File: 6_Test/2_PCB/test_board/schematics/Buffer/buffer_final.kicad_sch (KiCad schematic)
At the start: 24 parts, among them J11 Buffer_PWR_Jumper, U7 SN74ALVCH162827DLR

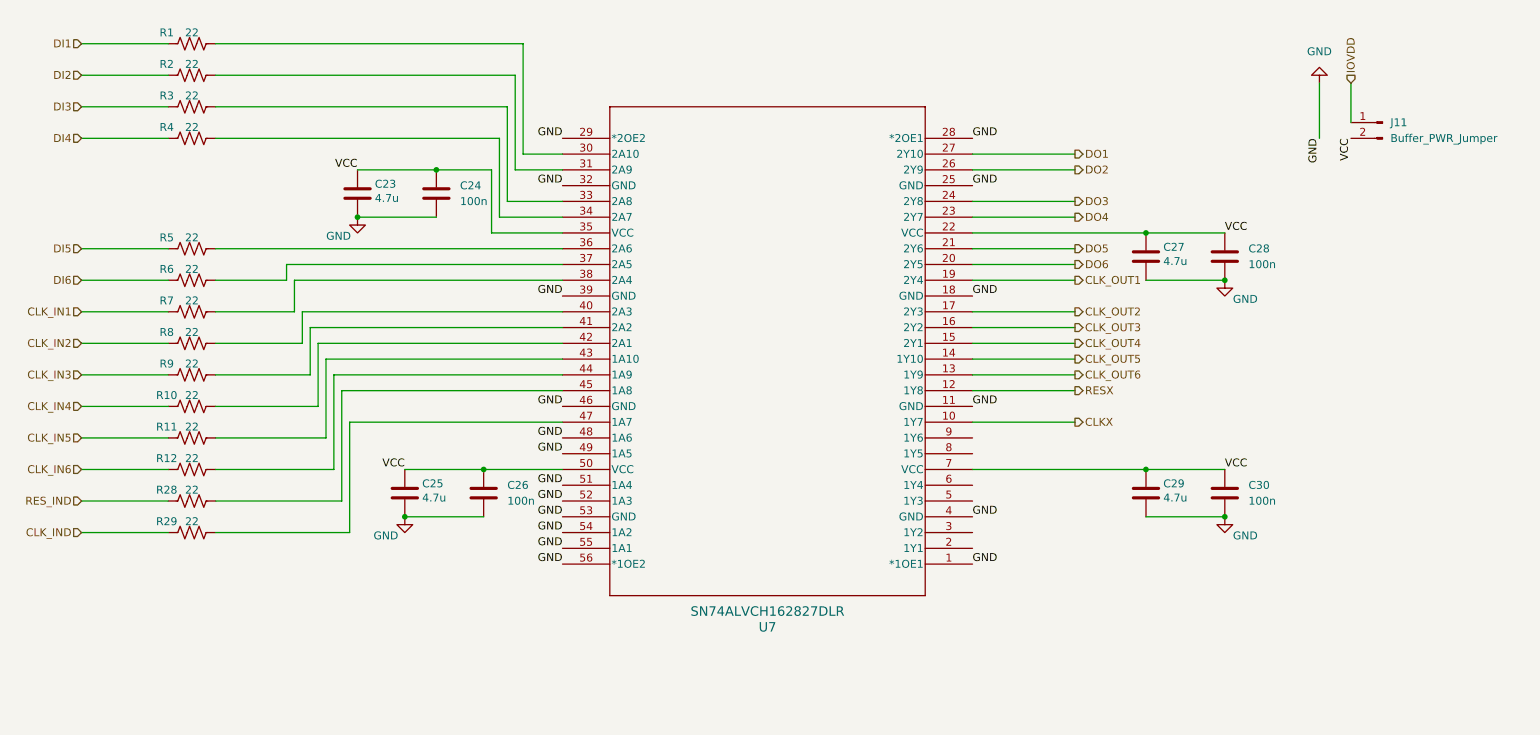
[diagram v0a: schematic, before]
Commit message: Edit Layout 1_27
Rearranged the components in the layout and added majority of traces and ground layer. AVSS connections still need to be connected along with IOVDD
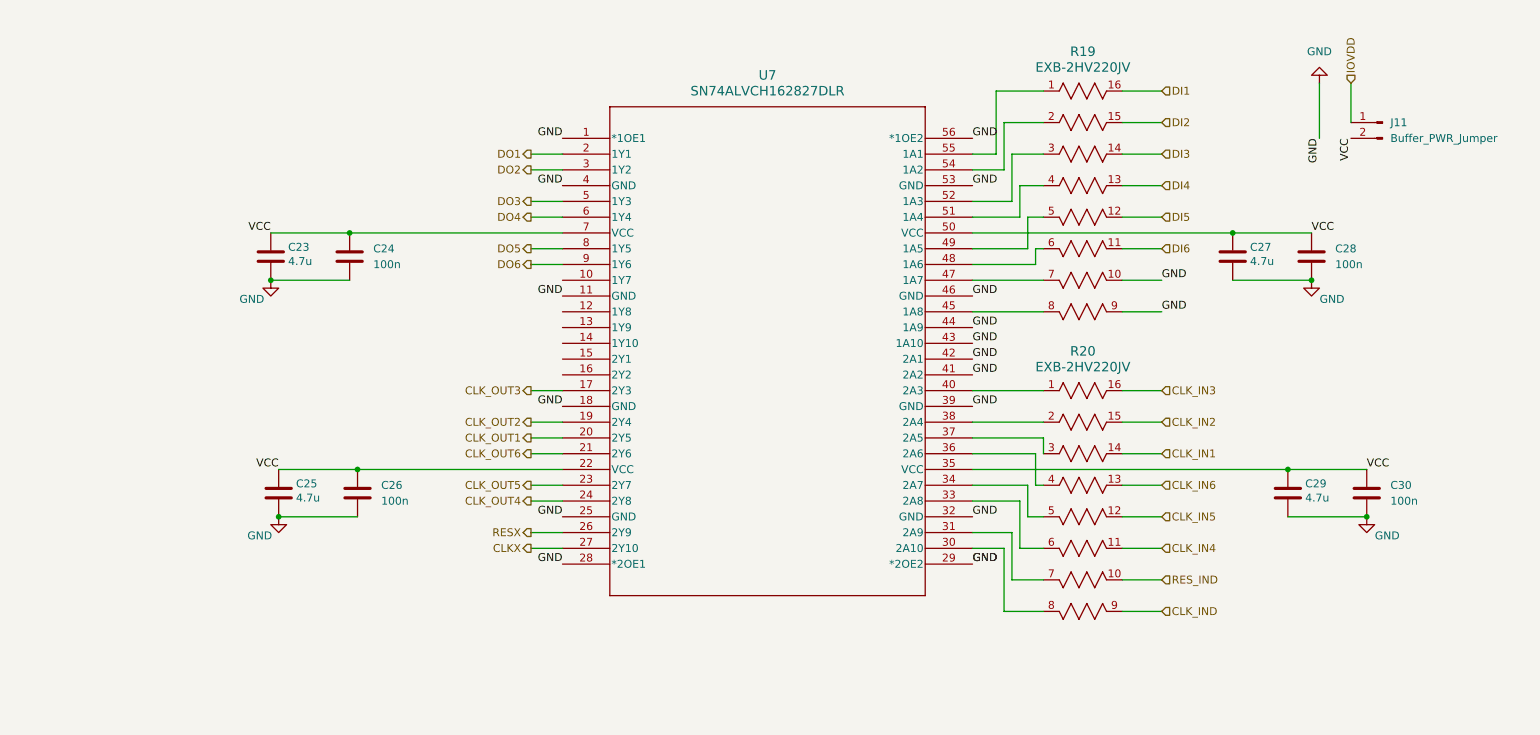
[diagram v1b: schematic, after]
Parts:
- removed R1, R10, R11, R12, R2, R28, R29, R3, R4, R5, R6, R7, R8, R9: 22, Resistor_SMD:R_0402_1005Metric, symbol Device:R_US
- added R19, R20: EXB-2HV220JV, 22res_arrayFootprints:RES_EXB2HV, symbol 22res_array:EXB-2HV220JV
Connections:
- net CLKX: now also U7.27 (2Y10); no longer U7.10 (1Y7)
- net CLK_IN1: now also R20.14
- net CLK_IN2: now also R20.15
- net CLK_IN3: now also R20.16
- net CLK_IN4: now also R20.11
- net CLK_IN5: now also R20.12
- net CLK_IN6: now also R20.13
- net CLK_IND: now also R20.9
- net CLK_OUT1: now also U7.20 (2Y5); no longer U7.19 (2Y4)
- net CLK_OUT2: now also U7.19 (2Y4); no longer U7.17 (2Y3)
- net CLK_OUT3: now also U7.17 (2Y3); no longer U7.16 (2Y2)
- net CLK_OUT4: now also U7.24 (2Y8); no longer U7.15 (2Y1)
- net CLK_OUT5: now also U7.23 (2Y7); no longer U7.14 (1Y10)
- net CLK_OUT6: now also U7.21 (2Y6); no longer U7.13 (1Y9)
- net DI1: now also R19.16
- net DI2: now also R19.15
- net DI3: now also R19.14
- net DI4: now also R19.13
- net DI5: now also R19.12
- net DI6: now also R19.11
- net DO1: now also U7.2 (1Y1); no longer U7.27 (2Y10)
- net DO2: now also U7.3 (1Y2); no longer U7.26 (2Y9)
- net DO3: now also U7.5 (1Y3); no longer U7.24 (2Y8)
- net DO4: now also U7.6 (1Y4); no longer U7.23 (2Y7)
- net DO5: now also U7.8 (1Y5); no longer U7.21 (2Y6)
- net DO6: now also U7.9 (1Y6); no longer U7.20 (2Y5)
- net GND: now also U7.41 (2A2), U7.42 (2A1), U7.43 (1A10), U7.44 (1A9), R19.10, R19.9; no longer U7.48 (1A6), U7.49 (1A5), U7.51 (1A4), U7.52 (1A3), U7.54 (1A2), U7.55 (1A1)
- net RESX: now also U7.26 (2Y9); no longer U7.12 (1Y8)
- net RES_IND: now also R20.10
- net at U7.31 (2A9): now also R20.7
- net at U7.30 (2A10): now also R20.8
- net at U7.33 (2A8): now also R20.6
- net at U7.34 (2A7): now also R20.5
- net at U7.36 (2A6): now also R20.4
- net at U7.37 (2A5): now also R20.3
- net at U7.38 (2A4): now also R20.2
- net at U7.40 (2A3): now also R20.1
- net at U7.45 (1A8): now also R19.8
- net at U7.47 (1A7): now also R19.7
- new net: R19.6, U7.48 (1A6)
- new net: R19.5, U7.49 (1A5)
- new net: R19.4, U7.51 (1A4)
- new net: R19.3, U7.52 (1A3)
- new net: R19.2, U7.54 (1A2)
- new net: R19.1, U7.55 (1A1)
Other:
- moved on the sheet: C23, C24, C25, C26, C27, C28, C29, C30, U7

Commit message: Finished board layout
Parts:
- removed C27, C29: 4.7u, Capacitor_SMD:C_0603_1608Metric, symbol Device:C
- removed C28, C30: 100n, Capacitor_SMD:C_0402_1005Metric, symbol Device:C
- removed U7: SN74ALVCH162827DLR, 74ALVCHFootprints:DL56, symbol 74ALVCH:SN74ALVCH162827DLR
- added R21, R22: EXB-2HV220JV, 22res_arrayFootprints:RES_EXB2HV, symbol 22res_array:EXB-2HV220JV
- added U7: SN74LVC245APWR, SN74LVC245APWRFootprints:PW20, symbol SN74LVC245APWR:SN74LVC245APWR
- added U8: SN74LVC245APWR, PW20, symbol SN74LVC245APWR:SN74LVC245APWR
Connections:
- net CLKX: now also R20.8
- net CLK_IN1: now also R22.14; no longer R20.14
- net CLK_IN2: now also R22.15; no longer R20.15
- net CLK_IN3: now also R22.16; no longer R20.16
- net CLK_IN4: now also R22.11; no longer R20.11
- net CLK_IN5: now also R22.12; no longer R20.12
- net CLK_IN6: now also R22.13; no longer R20.13
- net CLK_IND: now also R22.9; no longer R20.9
- net CLK_OUT1: now also R20.3
- net CLK_OUT2: now also R20.2
- net CLK_OUT3: now also R20.1
- net CLK_OUT4: now also R20.6
- net CLK_OUT5: now also R20.5
- net CLK_OUT6: now also R20.4
- net DI1: now also R19.1; no longer R19.16
- net DI2: now also R19.2; no longer R19.15
- net DI3: now also R19.3; no longer R19.14
- net DI4: now also R19.4; no longer R19.13
- net DI5: now also R19.5; no longer R19.12
- net DI6: now also R19.6; no longer R19.11
- net DO1: now also R21.16
- net DO2: now also R21.15
- net DO3: now also R21.14
- net DO4: now also R21.13
- net DO5: now also R21.12
- net DO6: now also R21.11
- net GND: now also R19.7, R19.8, U7.10 (GND), U7.19 (*OE), U8.1 (DIR), U8.10 (GND), U8.19 (*OE); no longer R19.10, R19.9
- net RESX: now also R20.7
- net RES_IND: now also R22.10; no longer R20.10
- net VCC: now also U7.1 (DIR), U7.20 (VCC), U8.20 (VCC)
- new net: R19.10, U7.8 (A7)
- new net: R19.11, U7.7 (A6)
- new net: R19.12, U7.6 (A5)
- new net: R19.13, U7.5 (A4)
- new net: R19.14, U7.4 (A3)
- new net: R19.15, U7.3 (A2)
- new net: R19.16, U7.2 (A1)
- new net: R19.9, U7.9 (A8)
- new net: R20.10, U8.8 (A7)
- new net: R20.11, U8.7 (A6)
- new net: R20.12, U8.6 (A5)
- new net: R20.13, U8.5 (A4)
- new net: R20.14, U8.4 (A3)
- new net: R20.15, U8.3 (A2)
- new net: R20.16, U8.2 (A1)
- new net: R20.9, U8.9 (A8)
- new net: R21.1, U7.18 (B1)
- new net: R21.2, U7.17 (B2)
- new net: R21.3, U7.16 (B3)
- new net: R21.4, U7.15 (B4)
- new net: R21.5, U7.14 (B5)
- new net: R21.6, U7.13 (B6)
- new net: R21.7, U7.12 (B7)
- new net: R21.8, U7.11 (B8)
- new net: R22.1, U8.18 (B1)
- new net: R22.2, U8.17 (B2)
- new net: R22.3, U8.16 (B3)
- new net: R22.4, U8.15 (B4)
- new net: R22.5, U8.14 (B5)
- new net: R22.6, U8.13 (B6)
- new net: R22.7, U8.12 (B7)
- new net: R22.8, U8.11 (B8)
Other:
- moved on the sheet: J11
